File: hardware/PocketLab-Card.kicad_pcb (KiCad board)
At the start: 4 copper layers, 85.6 x 54 mm, 267 parts, among them J1 USB-C DATA/POWER, J2 microSD, J3 EXTERNAL 400uH LF COIL, J4 PROTECTED 1S LiPo 3.7V, J5 30-PIN 2.54mm DUPONT GRID, J8 ER-OLED0.42-1W 72x40 SSD1306B, Q1 AO3400A IR DRIVER, Q2 CSD16406Q3 DISCHARGE, Q3 CSD16406Q3 CHARGE, SW1 RESET, SW2 BOOT, SW3 UP, SW4 DOWN, SW5 MAIN POWER OFF / ON, SW6 PAIR, SW7 SELECT, U1 ESP32-S3-WROOM-1-N8R2, U10 BMI270 (FULL OPTION), U11 BMP390 (FULL OPTION), U12 PCF8563T, U13 TSOP75338WTR 38kHz, U14 BQ29700DSE, U15 TPS2553DBVR 500mA LIMIT, U16 USBLC6-4SC6Y, U17 TPS22919DCKR LF 5V LOAD SWITCH, U18 TCA9534PWR INTERNAL CONTROL, U19 SRV05-4MR6T1G SD ESD, U2 PN5321A3HN/C106, U20 SN74AHCT1G126DBVR RGB LEVEL S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, U21 SN74LV125ATPWR LF/SPI 3V3-TO-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, U22 SN74LVC1G126DBVR LF 5V-TO-3V3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, U23 ATECC608C-SSHDA-T, U24 SRV05-4MR6T1G J5 BUS ESD, U25 SRV05-4MR6T1G J5 SPI ESD, U3 E07-900MM10S 855-925MHz, U4 HTRC11001T/03EE,11 125kHz, U5 BQ24074RGTR, U6 TPS63070RNMR 3V3, U7 TPS61023DRLR 5V BOOST, U8 MAX17048G+T10, U9 TCA9535PWR, Y301 27.12MHz crystal (pins 2/4 sh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, Y501 4MHz 5V CMOS OSCILLATOR, Y701 32.768kHz CL=7pF

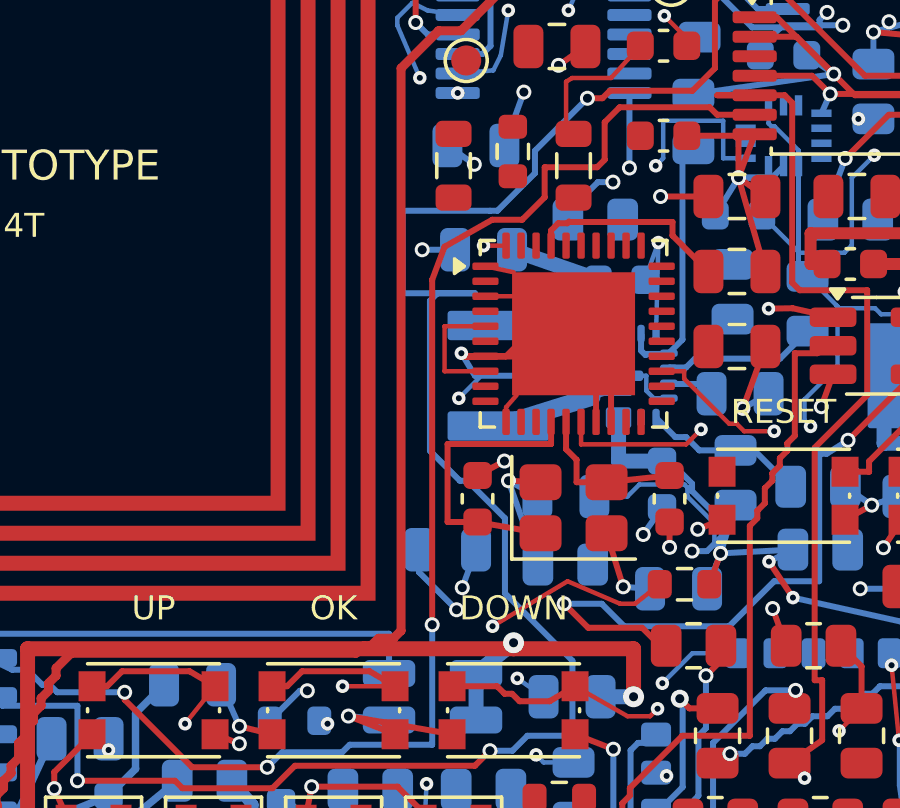
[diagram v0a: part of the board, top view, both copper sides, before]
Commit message: Route PN532 TX1 driver branch
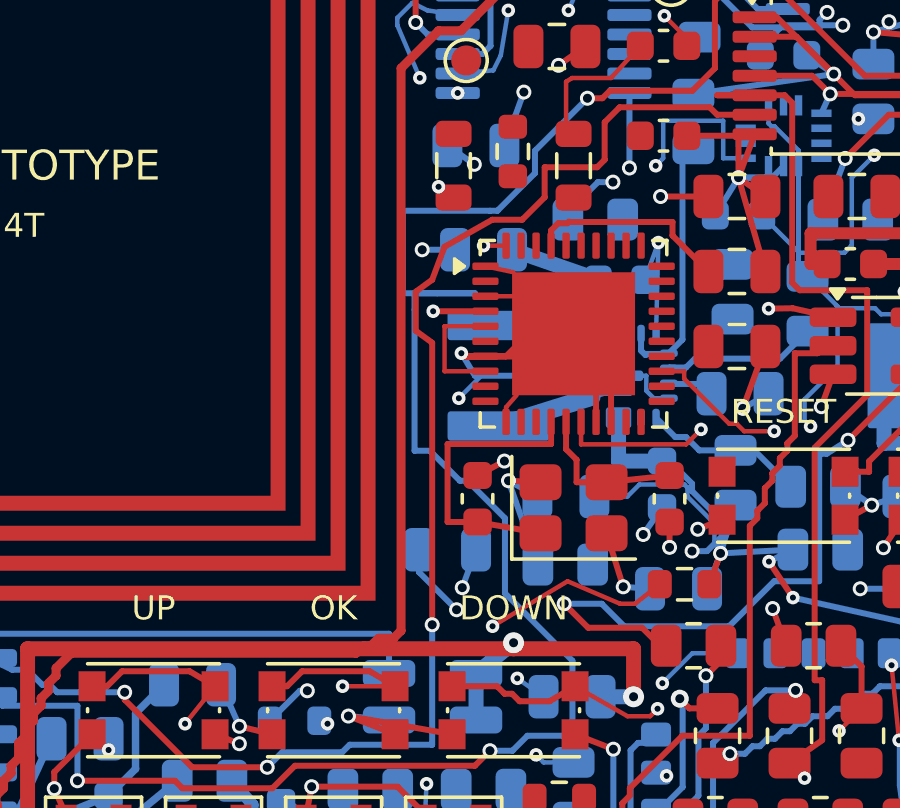
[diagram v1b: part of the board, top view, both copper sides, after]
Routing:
- net /NFC_TX1: track 0.00 -> 6.74 mm, vias 0 -> 2
- net /LF_DIN_5V: track 71.9 -> 73.1 mm
- net /LF_SCLK_5V: track 46.9 -> 47.5 mm
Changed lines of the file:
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@@
+	)
+	(segment
+		(start 60.32 41.85)
+		(end 62.0625 41.85)
+		(width 0.2)
+		(locked yes)
+		(layer "F.Cu")
+		(net "/NFC_TX1")
+	)
+	(segment
+		(start 61 38.0625)
+		(end 60.5 37.7)
+		(width 0.2)
+		(locked yes)
+		(layer "F.Cu")
+		(net "/NFC_TX1")
+	)
+	(via
+		(at 60.5 37.7)
+		(size 0.45)
+		(drill 0.2)
+		(layers "F.Cu" "B.Cu")
+		(locked yes)
+		(net "/NFC_TX1")
+	)
+	(via
+		(at 60.32 41.85)
+		(size 0.45)
+		(drill 0.2)
+		(layers "F.Cu" "B.Cu")
+		(locked yes)
+		(net "/NFC_TX1")
+	)
+	(segment
+		(start 61 39)
+		(end 61 40.2)
+		(width 0.2)
+		(locked yes)
+		(layer "In2.Cu")
+		(net "/NFC_TX1")
+	)
+	(segment
+		(start 61 40.2)
+		(end 60.32 41.85)
+		(width 0.2)
+		(locked yes)
+		(layer "In2.Cu")
+		(net "/NFC_TX1")
+	)
+	(segment
+		(start 60.5 37.7)
+		(end 61 39)
+		(width 0.2)
+		(locked yes)
+		(layer "In2.Cu")
+		(net "/NFC_TX1")
 	)
 	(segment
@@
 	)
 	(segment
+		(start 60.287499 42.9)
+		(end 60.287499 52.3)
+		(width 0.2)
+		(locked yes)
+		(layer "F.Cu")
+		(net "/LF_SCLK_5V")
+	)
+	(segment
 		(start 63.287499 38.8)
 		(end 62.287499 38.8)
@@
 	)
 	(segment
+		(start 59.74 41.2)
+		(end 59.74 42.5)
+		(width 0.2)
+		(locked yes)
+		(layer "F.Cu")
+		(net "/LF_SCLK_5V")
+	)
+	(segment
 		(start 66.037499 35.55)
 		(end 66.037499 36.8)
@@
 	)
 	(segment
+		(start 59.74 42.5)
+		(end 60.287499 42.9)
+		(width 0.2)
+		(locked yes)
+		(layer "F.Cu")
+		(net "/LF_SCLK_5V")
+	)
+	(segment
 		(start 69.5375 35.05)
 		(end 66.537499 35.05)
@@
 	(segment
 		(start 60.287499 40.8)
-		(end 60.287499 52.3)
+		(end 59.74 41.2)
 		(width 0.2)
 		(locked yes)
@@
 	(segment
 		(start 60.4625 41.25)
-		(end 60.2125 41.5)
+		(end 59.7 41.25)
 		(width 0.2)
 		(locked yes)
@@
 	)
 	(segment
+		(start 59.7 46.5)
+		(end 60.2125 46.5)
+		(width 0.2)
+		(locked yes)
+		(layer "B.Cu")
+		(net "/LF_DIN_5V")
+	)
+	(segment
 		(start 64.9625 55.75)
 		(end 64.7125 56)
@@
 	)
 	(segment
+		(start 59.7 41.25)
+		(end 59.7 41.8)
+		(width 0.2)
+		(locked yes)
+		(layer "B.Cu")
+		(net "/LF_DIN_5V")
+	)
+	(segment
 		(start 65.4625 34.75)
 		(end 63.7125 36.5)
@@
 	)
 	(segment
-		(start 60.2125 41.5)
-		(end 60.2125 46.5)
-		(width 0.2)
-		(locked yes)
+		(start 59.7 41.8)
+		(end 59.7 46.5)
+		(width 0.2)
+		(locked yes)

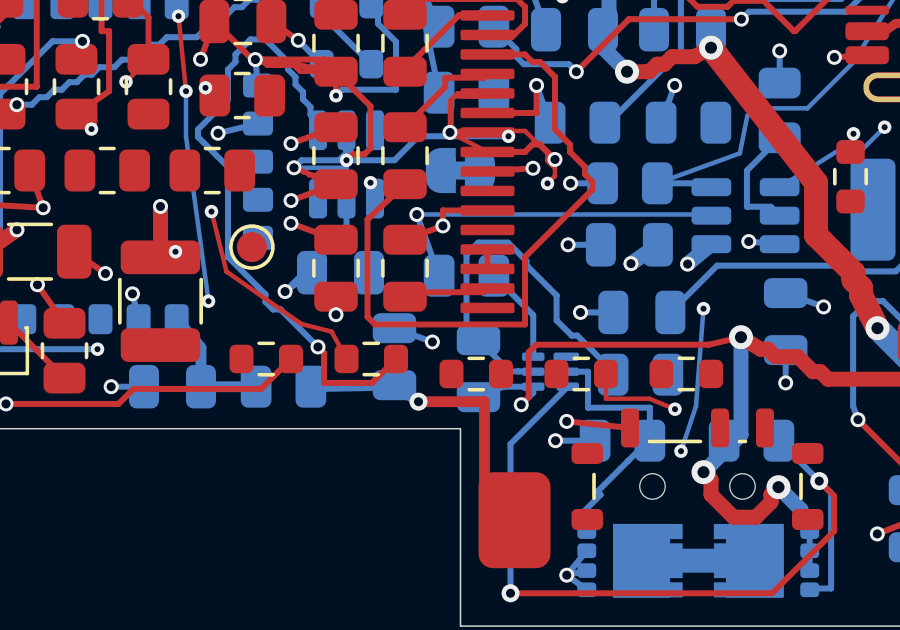
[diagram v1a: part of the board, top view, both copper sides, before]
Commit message: Route OLED VCC supply branch
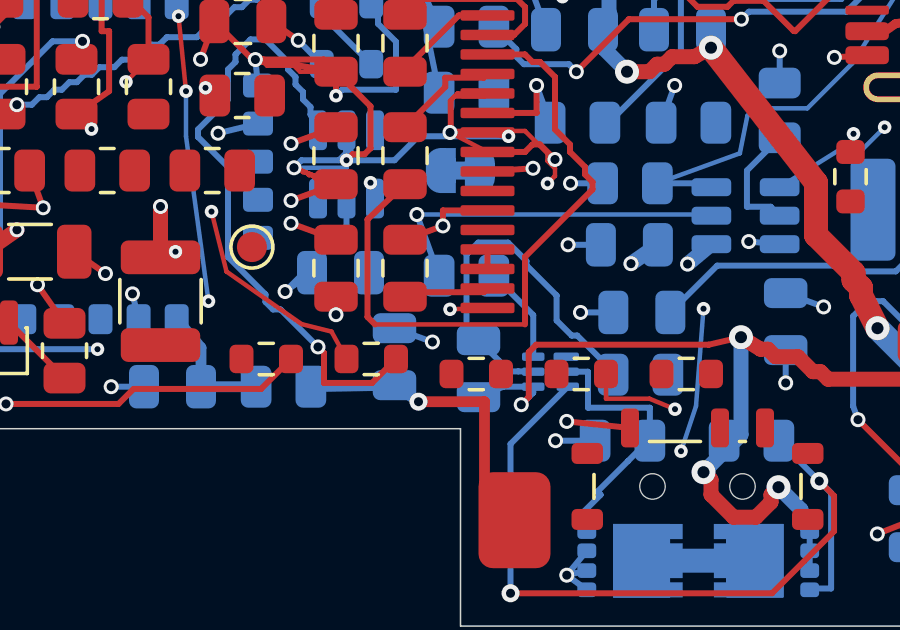
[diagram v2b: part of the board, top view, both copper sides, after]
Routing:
- net /OLED_VCC: track 2.38 -> 7.44 mm, vias 1 -> 2
- net /+5V_AUX: track 33.0 -> 36.9 mm
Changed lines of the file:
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@@
 		(start 87.15 63.925)
 		(end 82.15 63.925)
-		(width 0.2)
+		(width 0.15)
 		(locked yes)
 		(layer "F.Cu")
@@
 		(locked yes)
 		(layer "F.Cu")
+		(net "/OLED_VCC")
+	)
+	(segment
+		(start 84.65 63.42)
+		(end 85.9 63.375)
+		(width 0.15)
+		(locked yes)
+		(layer "F.Cu")
+		(net "/OLED_VCC")
+	)
+	(via
+		(at 84.65 63.42)
+		(size 0.45)
+		(drill 0.2)
+		(layers "F.Cu" "B.Cu")
+		(locked yes)
 		(net "/OLED_VCC")
 	)
@@
 		(locked yes)
 		(layer "B.Cu")
+		(net "/OLED_VCC")
+	)
+	(segment
+		(start 80.85 63.6)
+		(end 84.65 63.42)
+		(width 0.15)
+		(locked yes)
+		(layer "In2.Cu")
 		(net "/OLED_VCC")
 	)
@@
 		(locked yes)
 		(layer "In2.Cu")
+		(net "/+5V_AUX")
+	)
+	(segment
+		(start 81 64.8)
+		(end 84.8 65.25)
+		(width 0.2)
+		(locked yes)
+		(layer "In2.Cu")

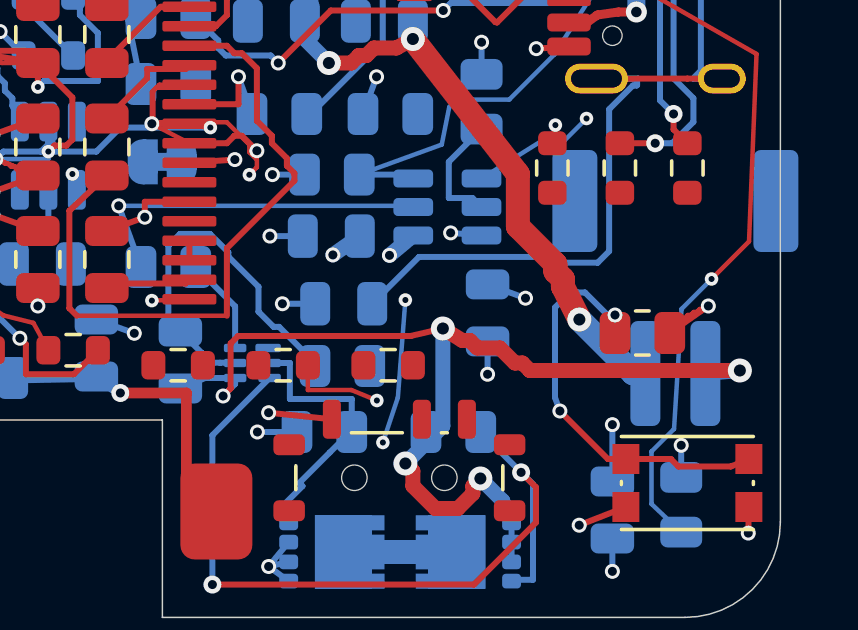
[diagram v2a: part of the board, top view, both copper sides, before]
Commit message: Route CELL_POS sense branch
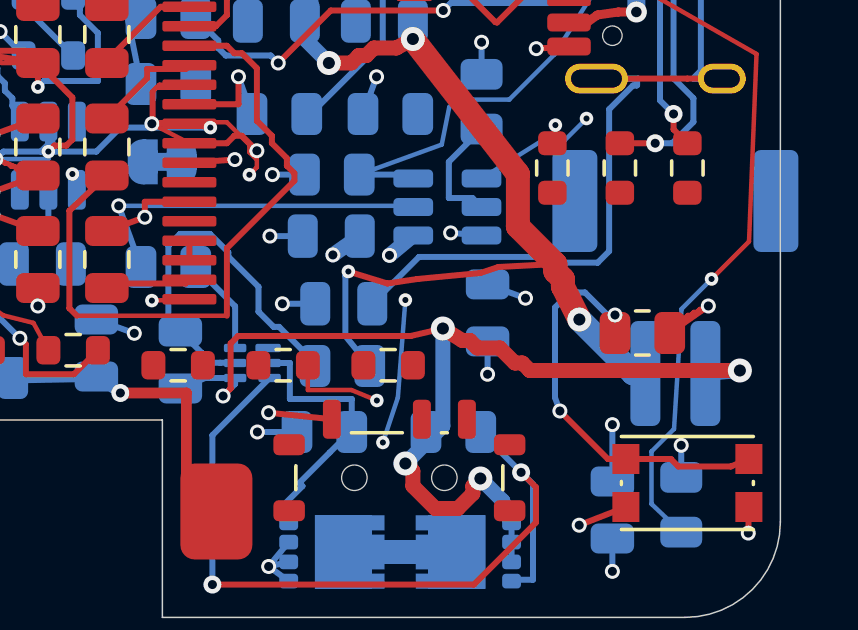
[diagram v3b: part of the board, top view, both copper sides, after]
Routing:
- net /CELL_POS: track 27.6 -> 38.1 mm, vias 3 -> 4
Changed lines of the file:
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@@
+	)
+	(segment
+		(start 96.2 62.3)
+		(end 98.1 62.2)
+		(width 0.2)
+		(locked yes)
+		(layer "F.Cu")
+		(net "/CELL_POS")
 	)
 	(segment
@@
 	)
 	(segment
+		(start 95.6 62.5)
+		(end 96.2 62.3)
+		(width 0.2)
+		(locked yes)
+		(layer "F.Cu")
+		(net "/CELL_POS")
+	)
+	(segment
 		(start 98.35 62.95)
 		(end 98.9 64.05)
@@
 	)
 	(segment
+		(start 93.5 62.7)
+		(end 95.6 62.5)
+		(width 0.2)
+		(locked yes)
+		(layer "F.Cu")
+		(net "/CELL_POS")
+	)
+	(segment
 		(start 90.55 55.5)
 		(end 91.3 55.5)
@@
 		(locked yes)
 		(layer "F.Cu")
+		(net "/CELL_POS")
+	)
+	(segment
+		(start 91.2 62.45)
+		(end 92.5 62.85)
+		(width 0.2)
+		(locked yes)
+		(layer "F.Cu")
+		(net "/CELL_POS")
+	)
+	(segment
+		(start 92.5 62.85)
+		(end 93.5 62.7)
+		(width 0.2)
+		(locked yes)
+		(layer "F.Cu")
+		(net "/CELL_POS")
+	)
+	(via
+		(at 91.2 62.45)
+		(size 0.45)
+		(drill 0.2)
+		(layers "F.Cu" "B.Cu")
+		(locked yes)
 		(net "/CELL_POS")
 	)
@@
 	)
 	(segment
+		(start 91.9125 65.599999)
+		(end 91.1 64.599999)
+		(width 0.2)
+		(locked yes)
+		(layer "B.Cu")
+		(net "/CELL_POS")
+	)
+	(segment
 		(start 90.45 51.9375)
 		(end 90.45 53)
@@
 		(end 89.75 54.7)
 		(width 0.5)
+		(locked yes)
+		(layer "B.Cu")
+		(net "/CELL_POS")
+	)
+	(segment
+		(start 91.1 64.599999)
+		(end 91.1 62.6)
+		(width 0.2)
 		(locked yes)
 		(layer "B.Cu")
@@
 		(locked yes)
 		(layer "B.Cu")
+		(net "/CELL_POS")
+	)
+	(segment
+		(start 91.1 62.6)
+		(end 91.2 62.45)
+		(width 0.2)
+		(locked yes)
+		(layer "B.Cu")

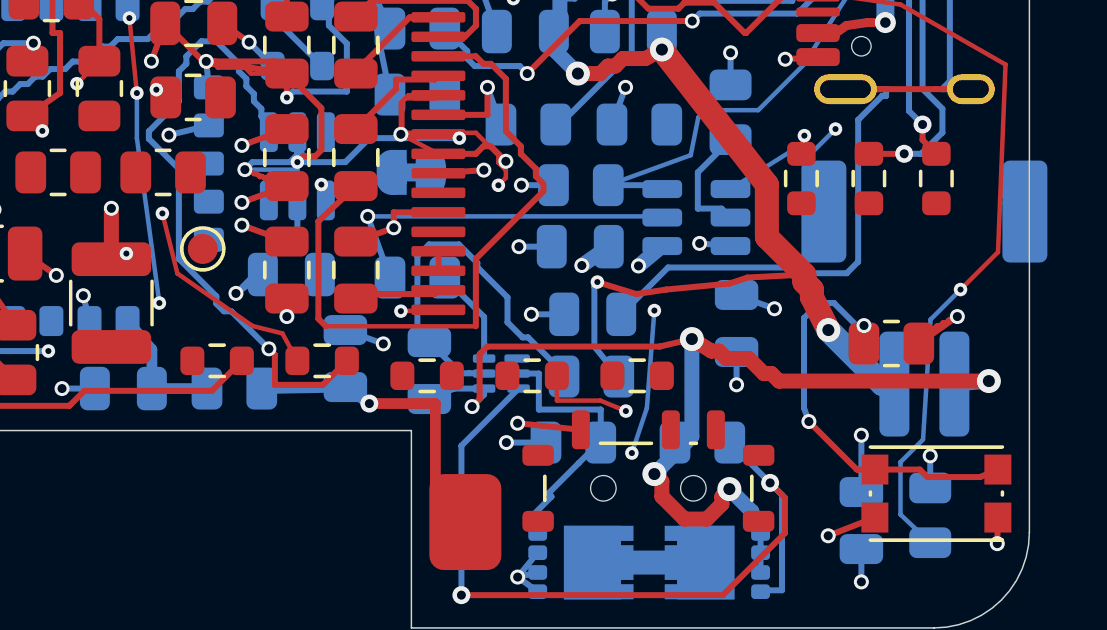
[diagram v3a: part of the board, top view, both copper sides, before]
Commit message: Place CELL_NEG test point on routed trunk
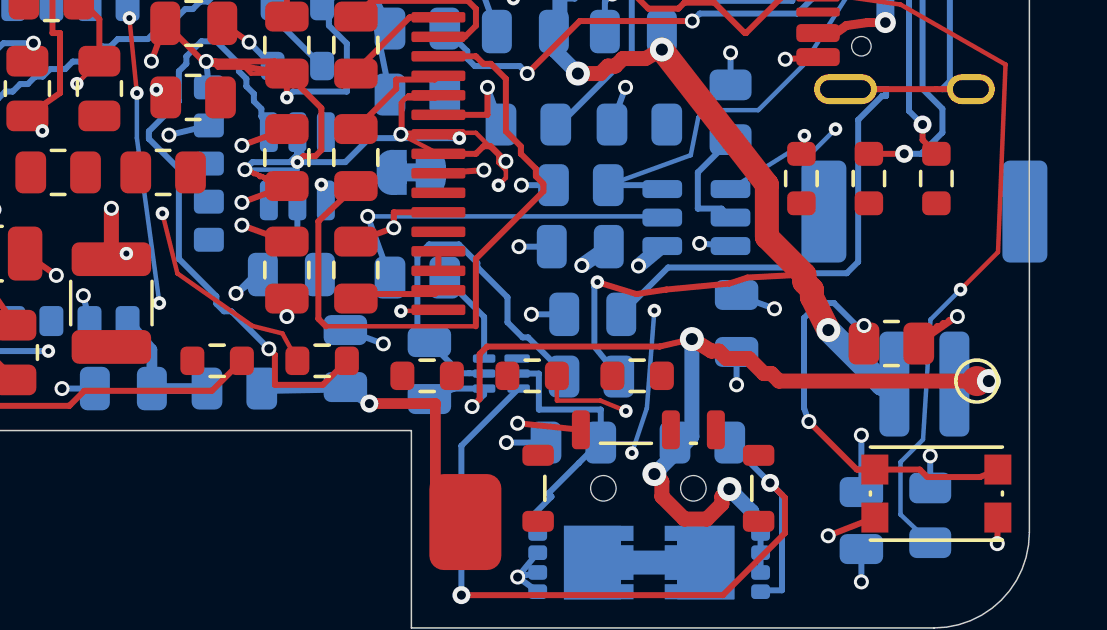
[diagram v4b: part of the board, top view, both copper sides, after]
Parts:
- moved TP102 26.2 mm to (103.8, 65.8)
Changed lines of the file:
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@@
 	)
 	(footprint "TestPoint:TestPoint_Pad_D1.0mm"
+		(locked yes)
 		(layer "F.Cu")
-		(at 78.047277 61.346)
+		(at 103.85 65.75)
 		(descr "SMD pad as test Point, diameter 1.0mm")
 		(tags "test point SMD pad")

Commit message: Place CELL_POS test point on routed trunk
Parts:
- moved TP101 73.3 mm to (98.1, 62.2)
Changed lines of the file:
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@@
 	)
 	(footprint "TestPoint:TestPoint_Pad_D1.0mm"
+		(locked yes)
 		(layer "F.Cu")
-		(at 36.5473 22.346)
+		(at 98.1 62.2)
 		(descr "SMD pad as test Point, diameter 1.0mm")
 		(tags "test point SMD pad")

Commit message: Place VBUS_USB test point on back trunk
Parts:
- TP105: moved to B.Cu
- moved TP105 50.1 mm to (99.0, 50.4), turned to 180 degrees
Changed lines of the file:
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@@
 		)
 	)
-	(footprint "TestPoint:TestPoint_Pad_D1.0mm"
-		(layer "F.Cu")
-		(at 57.547277 22.346)
-		(descr "SMD pad as test Point, diameter 1.0mm")
-		(tags "test point SMD pad")
-		(property "Reference" "TP105"
-			(at -0.001278 -1.426273 0)
-			(layer "F.Fab")
-			(effects
-				(font
-					(size 0.8 0.8)
-					(thickness 0.12)
-				)
-			)
-		)
-		(property "Value" "POWER VBUS_USB"
-			(at 0 1.55 0)
-			(layer "F.Fab")
-			(hide yes)
-			(effects
-				(font
-					(size 1 1)
-					(thickness 0.15)
-				)
-			)
-		)
-		(property "Datasheet" ""
-			(at 0 0 0)
-			(unlocked yes)
-			(layer "F.Fab")
-			(hide yes)
-			(effects
-				(font
-					(size 1.27 1.27)
-					(thickness 0.15)
-				)
-			)
-		)
-		(property "Description" ""
-			(at 0 0 0)
-			(unlocked yes)
-			(layer "F.Fab")
-			(hide yes)
-			(effects
-				(font
-					(size 1.27 1.27)
-					(thickness 0.15)
-				)
-			)
-		)
-		(attr exclude_from_pos_files exclude_from_bom)
-		(duplicate_pad_numbers_are_jumpers no)
-		(fp_circle
-			(center 0 0)
-			(end 0 0.7)
-			(stroke
-				(width 0.12)
-				(type solid)
-			)
-			(fill no)
-			(layer "F.SilkS")
-		)
-		(fp_circle
-			(center 0 0)
-			(end 1 0)
-			(stroke
-				(width 0.05)
-				(type solid)
-			)
-			(fill no)
-			(layer "F.CrtYd")
-		)
-		(fp_text user "${REFERENCE}"
-			(at 0 -1.45 0)
-			(layer "F.Fab")
-			(effects
-				(font
-					(size 1 1)
-					(thickness 0.15)
-				)
-			)
-		)
-		(pad "1" smd circle
-			(at 0 0)
-			(size 1 1)
-			(layers "F.Cu" "F.Mask")
-			(net "/VBUS_USB")
-		)
-		(embedded_fonts no)
-	)
 	(footprint "Package_TO_SOT_SMD:SOT-363_SC-70-6"
 		(layer "F.Cu")
@@
 		)
 	)
+	(footprint "TestPoint:TestPoint_Pad_D1.0mm"
+		(locked yes)
+		(layer "B.Cu")
+		(at 99 50.4 180)
+		(descr "SMD pad as test Point, diameter 1.0mm")
+		(tags "test point SMD pad")
+		(property "Reference" "TP105"
+			(at -0.001278 1.426273 0)
+			(layer "B.Fab")
+			(effects
+				(font
+					(size 0.8 0.8)
+					(thickness 0.12)
+				)
+				(justify mirror)
+			)
+		)
+		(property "Value" "POWER VBUS_USB"
+			(at 0 -1.55 0)
+			(layer "B.Fab")
+			(hide yes)
+			(effects
+				(font
+					(size 1 1)
+					(thickness 0.15)
+				)
+				(justify mirror)
+			)
+		)
+		(property "Datasheet" ""
+			(at 0 0 0)
+			(unlocked yes)
+			(layer "B.Fab")
+			(hide yes)
+			(effects
+				(font
+					(size 1.27 1.27)
+					(thickness 0.15)
+				)
+				(justify mirror)
+			)
+		)
+		(property "Description" ""
+			(at 0 0 0)
+			(unlocked yes)
+			(layer "B.Fab")
+			(hide yes)
+			(effects
+				(font
+					(size 1.27 1.27)
+					(thickness 0.15)
+				)
+				(justify mirror)
+			)
+		)
+		(attr exclude_from_pos_files exclude_from_bom)
+		(duplicate_pad_numbers_are_jumpers no)
+		(fp_circle
+			(center 0 0)
+			(end 0 -0.7)
+			(stroke
+				(width 0.12)
+				(type solid)
+			)
+			(fill no)
+			(layer "B.SilkS")
+		)
+		(fp_circle
+			(center 0 0)
+			(end 1 0)
+			(stroke
+				(width 0.05)
+				(type solid)
+			)
+			(fill no)
+			(layer "B.CrtYd")
+		)
+		(fp_text user "${REFERENCE}"
+			(at 0 1.45 0)
+			(layer "B.Fab")
+			(effects
+				(font
+					(size 1 1)
+					(thickness 0.15)
+				)
+				(justify mirror)
+			)
+		)
+		(pad "1" smd circle
+			(at 0 0 180)
+			(size 1 1)
+			(layers "B.Cu" "B.Mask")
+			(net "/VBUS_USB")
+		)
+		(embedded_fonts no)
+	)
 	(footprint "Capacitor_SMD:C_0805_2012Metric"
